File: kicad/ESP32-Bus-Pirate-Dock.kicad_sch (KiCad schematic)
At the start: 18 parts, among them CN1 HX25418-10WA, J1 Conn_01x10V, J2 Conn_01x22, J3 Conn_01x22, J4 Conn_02x03, J5 Conn_01x22, J6 Conn_01x22, J7 Conn_01x22, U1 ESP32-S3-DEVKITC-1-N8R2, U4 TLV75518PDBV

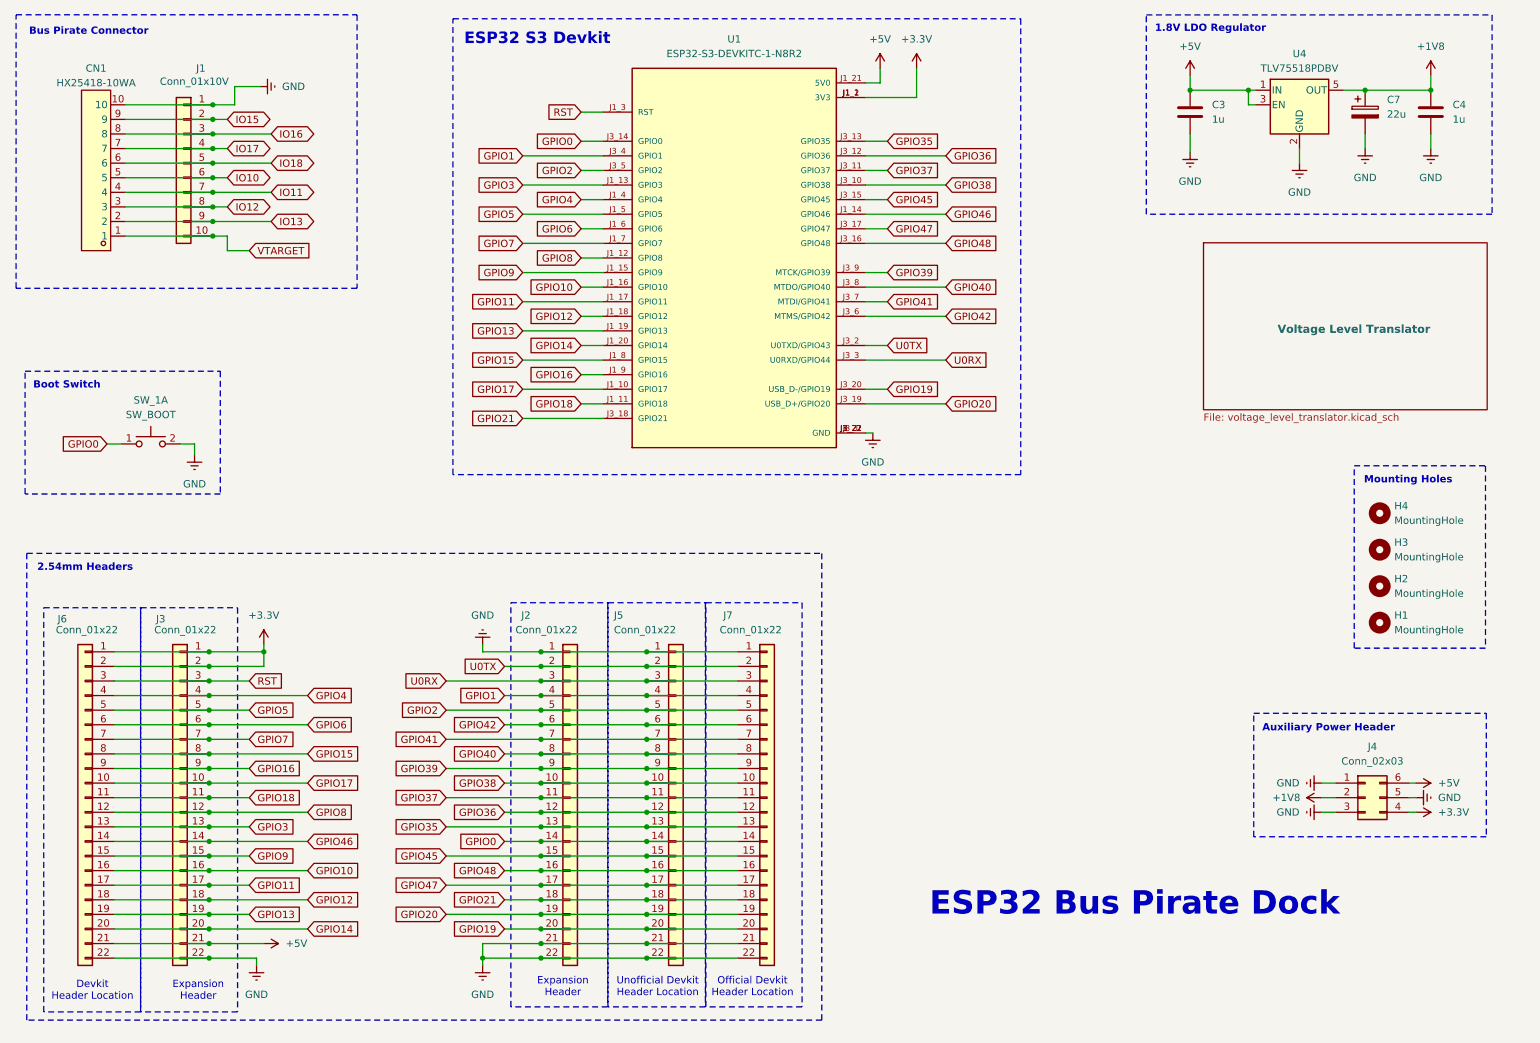
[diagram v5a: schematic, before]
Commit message: Minor pcb modifications
- Modified capacitors for multiplexers to 4.7u
- Added bypass capacitors near  TXS0108EPW VCCA and VCCB
- Changed some text on the main schematic
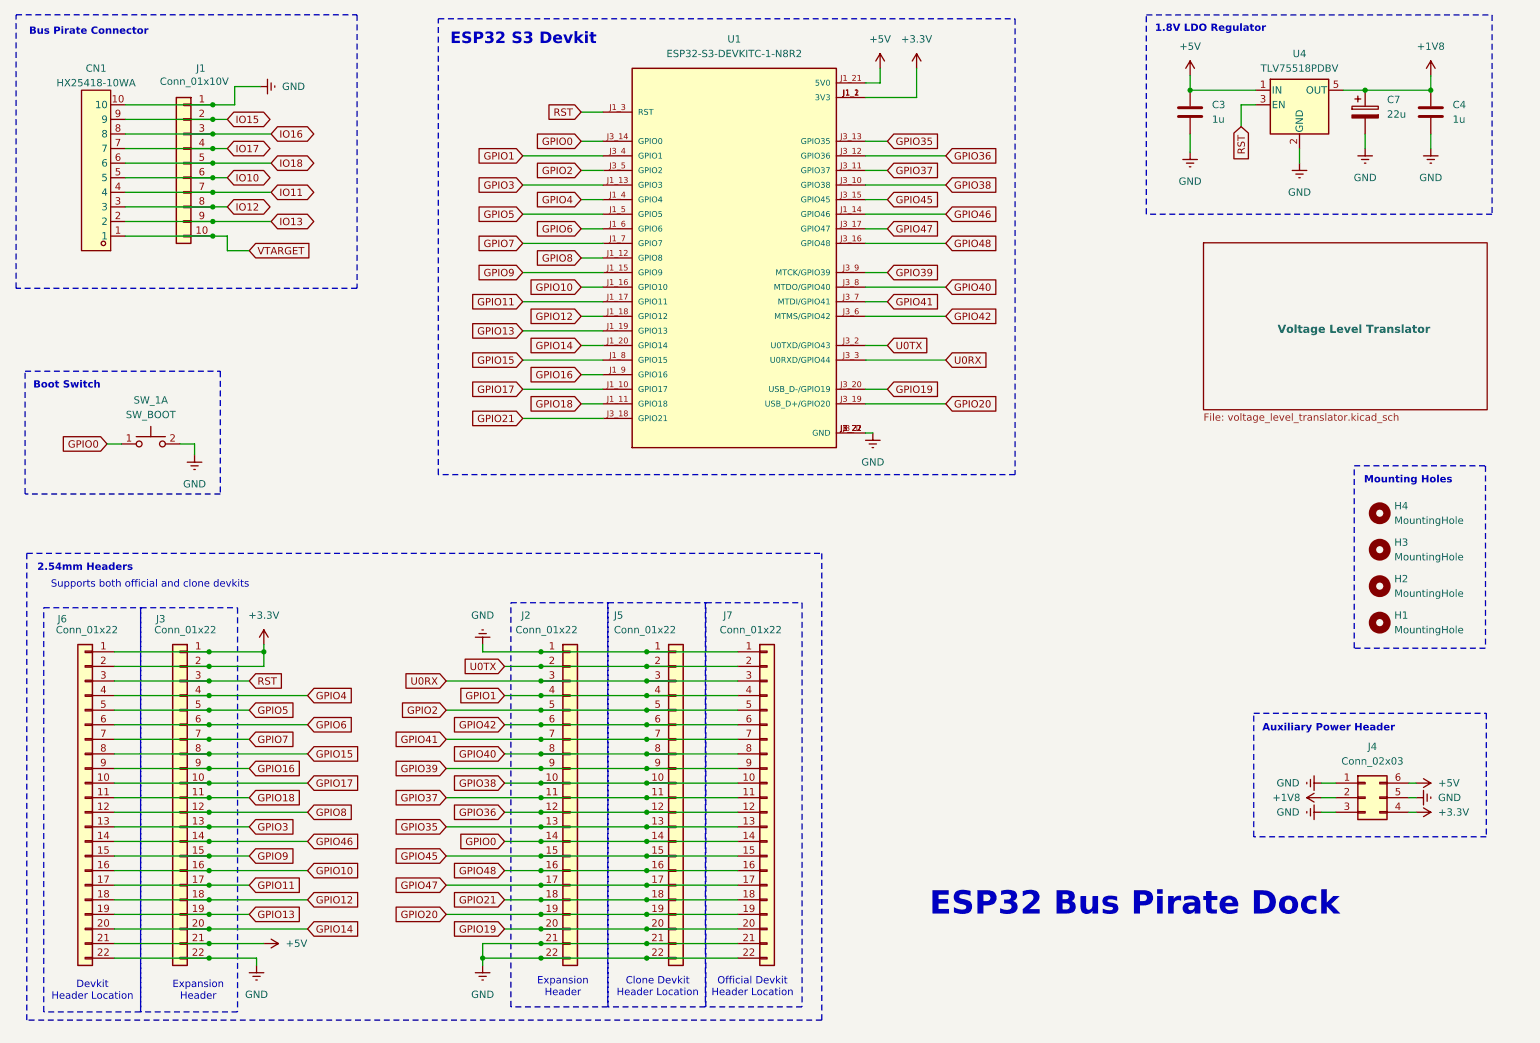
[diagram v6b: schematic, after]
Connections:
- net +5V: no longer U4.3 (EN)
- net RST: now also U4.3 (EN)
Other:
- note added: "Clone Devkit Header Location"
- note added: "Supports both official and clone devkits"
- note removed: "Unofficial Devkit Header Location"
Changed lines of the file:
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@@
 	)
 	(rectangle
-		(start 96.425 18.04)
-		(end 195.3 97.415)
+		(start 93.885 18.04)
+		(end 194.31 97.415)
 		(stroke
 			(width 0)
@@
 		)
 	)
-	(text "Unofficial Devkit \nHeader Location"
+	(text "Clone Devkit \nHeader Location"
 		(exclude_from_sim no)
 		(at 132.08 186.69 0)
@@
 	(text "ESP32 S3 Devkit"
 		(exclude_from_sim no)
-		(at 111.125 21.59 0)
+		(at 108.712 21.59 0)
 		(effects
 			(font
@@
 				(thickness 0.254)
 				(bold yes)
+				(color 132 132 0 1)
+			)
+		)
+	)
+	(text "Supports both official and clone devkits"
+		(exclude_from_sim no)
+		(at 43.688 116.586 0)
+		(effects
+			(font
+				(size 1.27 1.27)
 				(color 132 132 0 1)
 			)
@@
 	)
 	(junction
-		(at 234.95 30.48)
-		(diameter 0)
-		(color 0 0 0 0)
-	)
-	(junction
 		(at 130.175 135.89)
 		(diameter 0)
@@
 	(wire
 		(pts
-			(xy 236.22 30.48) (xy 234.95 30.48)
-		)
-		(stroke
-			(width 0)
-			(type default)
-		)
-	)
-	(wire
-		(pts
 			(xy 57.15 55.88) (xy 54.61 55.88)
 		)
@@
 	(wire
 		(pts
-			(xy 234.95 33.02) (xy 234.95 30.48)
-		)
-		(stroke
-			(width 0)
-			(type default)
-		)
-	)
-	(wire
-		(pts
 			(xy 108.585 82.55) (xy 122.555 82.55)
 		)
@@
 	(wire
 		(pts
+			(xy 233.68 36.83) (xy 233.68 33.02)
+		)
+		(stroke
+			(width 0)
+			(type default)
+		)
+	)
+	(wire
+		(pts
 			(xy 111.76 179.07) (xy 130.175 179.07)
 		)
@@
 	(wire
 		(pts
-			(xy 224.79 30.48) (xy 234.95 30.48)
+			(xy 224.79 30.48) (xy 236.22 30.48)
 		)
 		(stroke
@@
 	(wire
 		(pts
+			(xy 233.68 33.02) (xy 236.22 33.02)
+		)
+		(stroke
+			(width 0)
+			(type default)
+		)
+	)
+	(wire
+		(pts
 			(xy 118.745 49.53) (xy 122.555 49.53)
 		)
@@
 		(pts
 			(xy 130.175 128.27) (xy 146.05 128.27)
-		)
-		(stroke
-			(width 0)
-			(type default)
-		)
-	)
-	(wire
-		(pts
-			(xy 234.95 33.02) (xy 236.22 33.02)
 		)
 		(stroke
@@
 			(effects
 				(font
+					(size 1.27 1.27)
+				)
+				(justify right)
+			)
+		)
+	)
+	(global_label "RST"
+		(shape input)
+		(at 233.68 36.83 270)
+		(fields_autoplaced yes)
+		(effects
+			(font
+				(size 1.27 1.27)
+			)
+			(justify right)
+		)
+		(property "Intersheetrefs" "${INTERSHEET_REFS}"
+			(at 233.68 43.2623 90)
+			(effects
+				(font

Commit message: Updated PCB placement
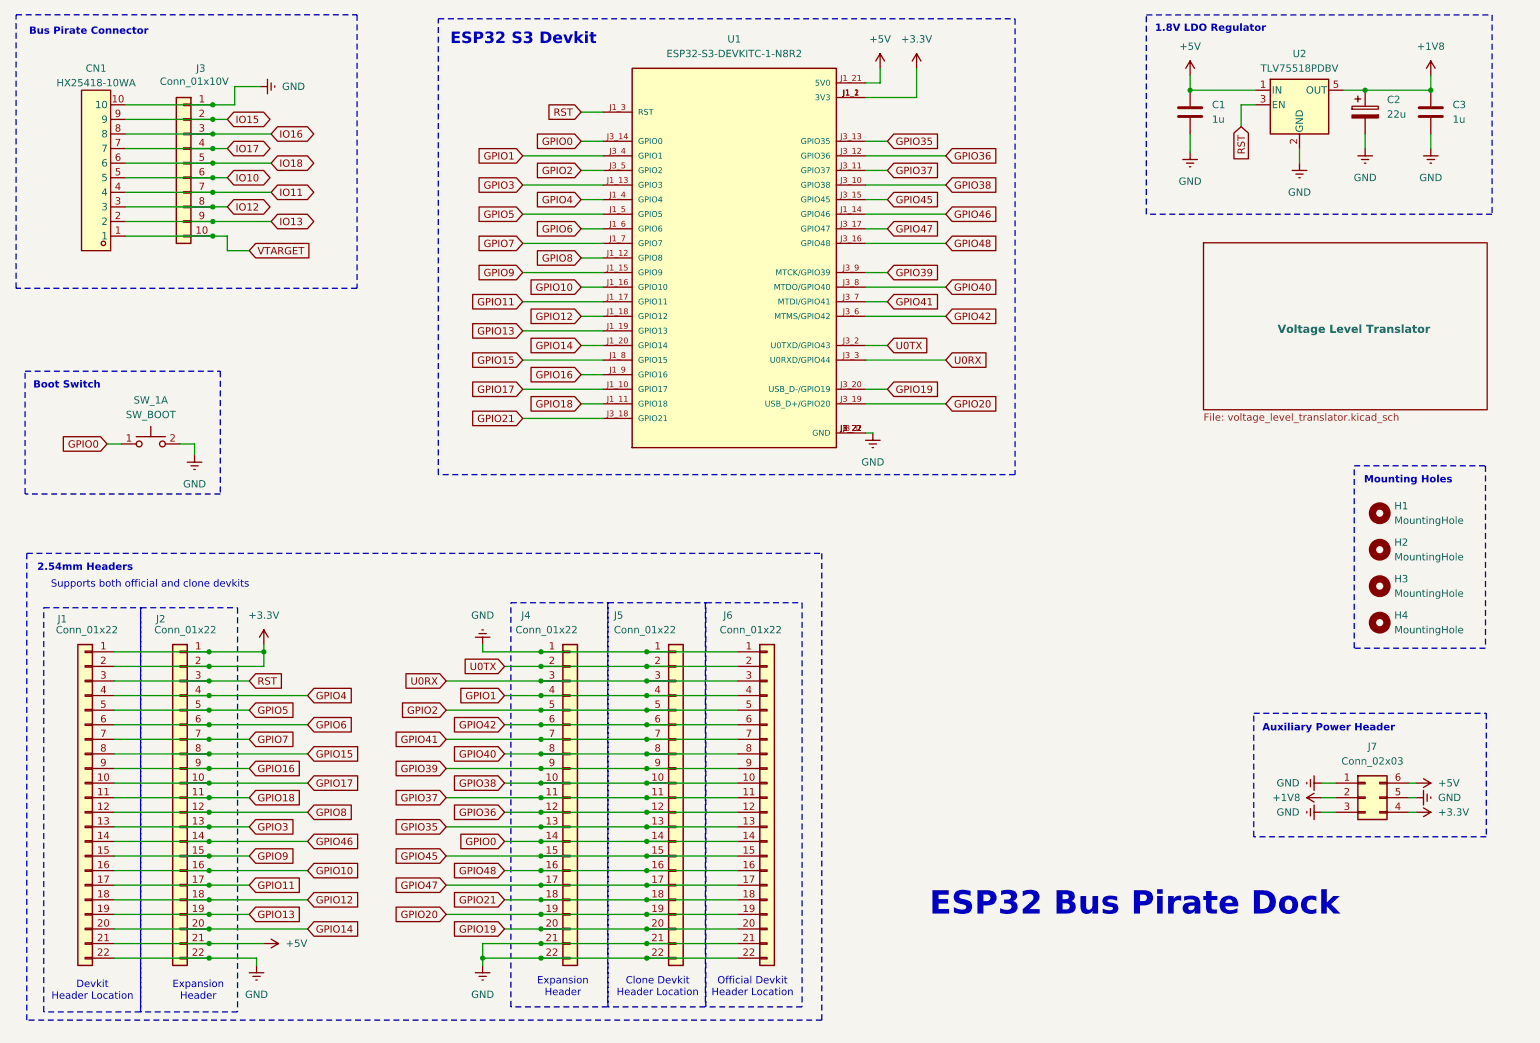
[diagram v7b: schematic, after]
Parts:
- renumbered C3 to C1, C7 to C2, C4 to C3, H4 to H1, H3 to H2, H2 to H3, H1 to H4, J6 to J1, J3 to J2, J1 to J3, J2 to J4, J7 to J6, J4 to J7, U4 to U2

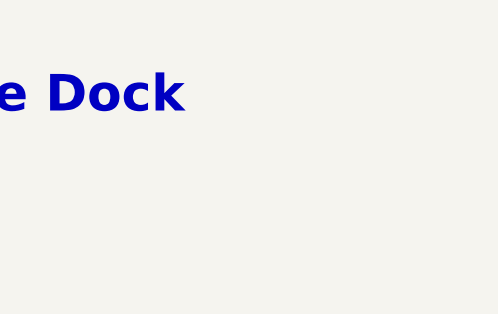
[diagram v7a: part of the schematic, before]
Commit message: Added board version
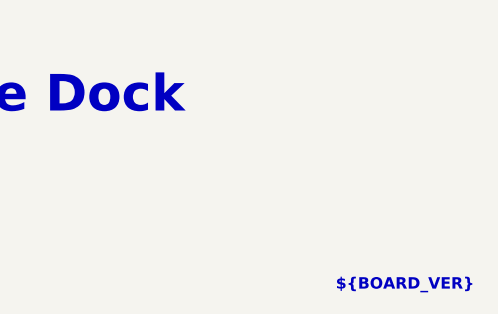
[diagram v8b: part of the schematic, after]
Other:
- note added: "${BOARD_VER}"
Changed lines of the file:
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@@
+		)
+	)
+	(text "${BOARD_VER}"
+		(exclude_from_sim no)
+		(at 275.336 193.294 0)
+		(effects
+			(font
+				(size 1.27 1.27)
+				(thickness 0.254)
+				(bold yes)
+				(color 132 0 0 1)
+			)
+			(href "#1")
 		)
 	)
